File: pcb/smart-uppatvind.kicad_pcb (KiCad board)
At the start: 4 copper layers, 74 x 36 mm, 65 parts, among them J1 PWR, J2 QWIIC, J3 UART_PROG, J4 FAN, Q1 IRLML9301, Q2 MMBT3904, Q3 MMBT3904, Q4 MMBT3904, Q5 Q_NMOS_GSD, SW1 EN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

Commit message: Fixed inverted signals on main connectors, added generated schematic
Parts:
- moved JP1 6.28 mm to (82.5, 66.0), turned to 180 degrees
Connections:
- J1 pad 1: GNDPWR -> +24V
- J1 pad 2: +24V -> GNDPWR
- J4 pad 1: /FG -> /FAN_24V
- J4 pad 2: /PWM_5V -> GND
- J4 pad 3: GND -> /PWM_5V
- J4 pad 4: /FAN_24V -> /FG
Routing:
- net /FAN_24V: track 11.5 -> 5.27 mm
- net Net-(JP1-B): track 24.8 -> 27.8 mm
- net /PWM_5V: track 24.4 -> 22.0 mm
- net /FG: track 7.47 -> 6.42 mm
- net +24V: track 12.2 -> 12.3 mm, vias 2 -> 7

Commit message: Formatted some resistor values
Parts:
- R10, R20, R7, R9: value 330 R -> 330R
- R13, R17: value 5.1kR -> 5.1k
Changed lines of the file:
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@@
 			)
 		)
-		(property "Value" "330 R"
+		(property "Value" "330R"
 			(at 0 1.65 0)
 			(layer "F.Fab")
@@
 			)
 		)
-		(property "Value" "330 R"
+		(property "Value" "330R"
 			(at 0 1.65 0)
 			(layer "F.Fab")
@@
 			)
 		)
-		(property "Value" "330 R"
+		(property "Value" "330R"
 			(at 0 1.65 0)
 			(layer "F.Fab")
@@
 			)
 		)
-		(property "Value" "5.1kR"
+		(property "Value" "5.1k"
 			(at 0 1.65 90)
 			(layer "F.Fab")
@@
 			)
 		)
-		(property "Value" "330 R"
+		(property "Value" "330R"
 			(at 0 1.65 0)
 			(layer "F.Fab")
@@
 			)
 		)
-		(property "Value" "5.1kR"
+		(property "Value" "5.1k"
 			(at 0 1.65 90)
 			(layer "F.Fab")

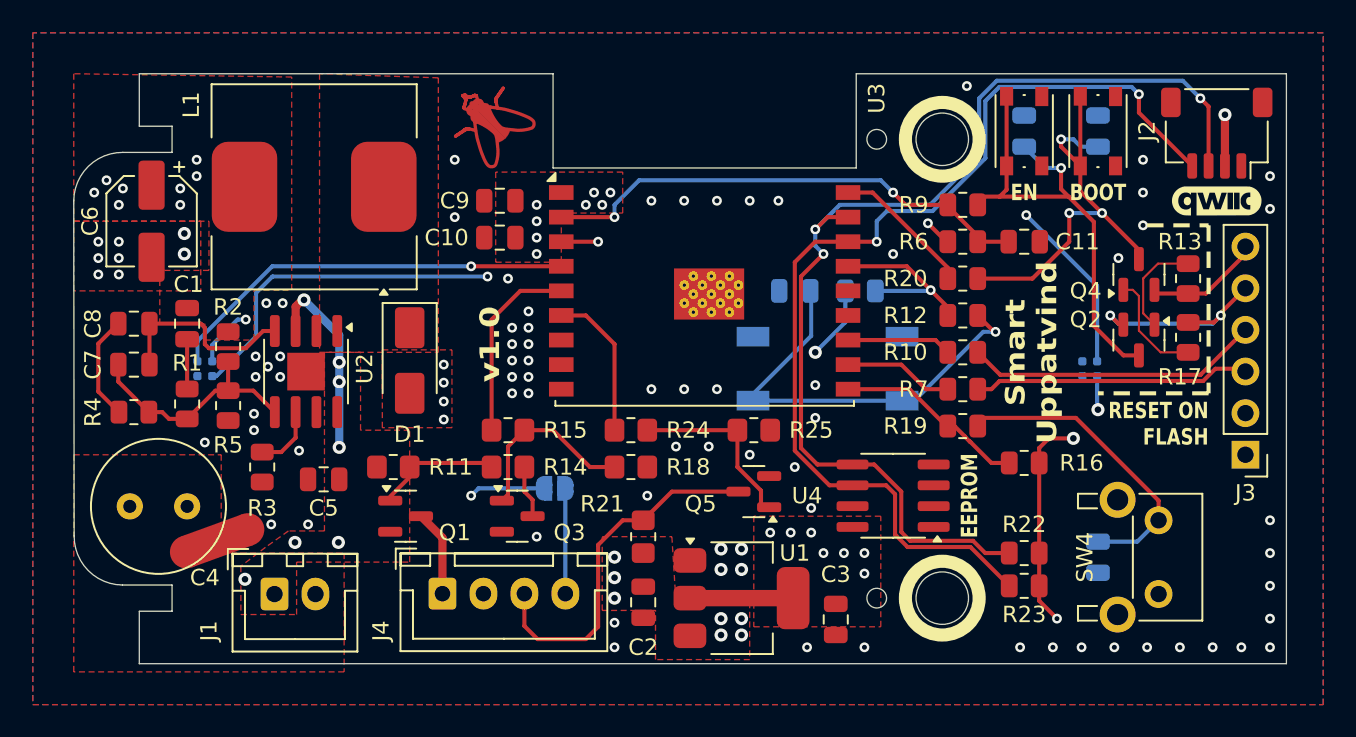
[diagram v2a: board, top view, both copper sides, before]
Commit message: Fixed incorrect connection of strapping pins for ESP32-C3
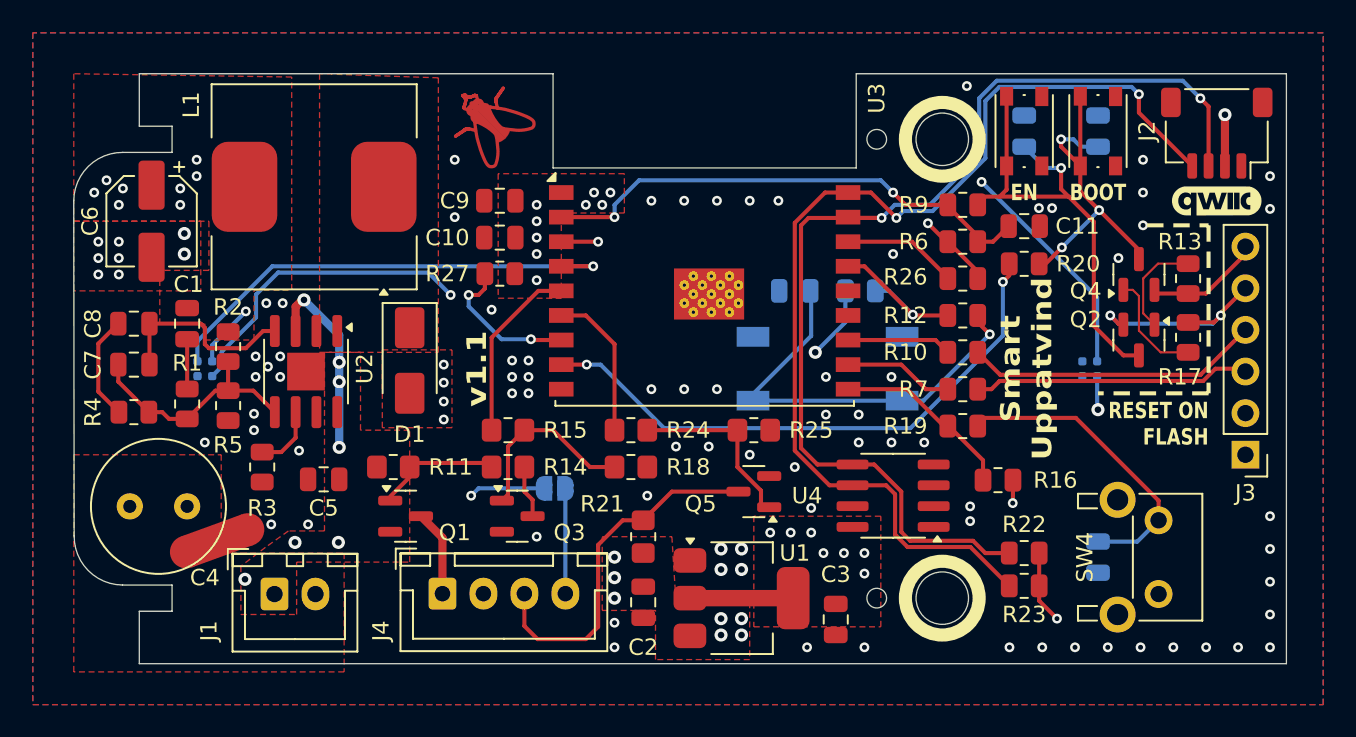
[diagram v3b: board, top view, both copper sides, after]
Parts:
- added R26: 100k, Resistor_SMD:R_0805_2012Metric, F.Cu at (107.3, 53.2)
- added R27: 100k, Resistor_SMD:R_0805_2012Metric, F.Cu at (79.1, 52.9)
- moved R20 3.86 mm to (111.1, 52.3)
- moved R16 1.91 mm to (109.5, 65.5)
- moved C11 0.95 mm to (111.1, 50.0)
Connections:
- U3 pad 16: /SCL -> Net-(U3-IO2)
- U3 pad 18: /BOOT -> /SCL
- U3 pad 7: unconnected-(U3-IO8-Pad7) -> Net-(U3-IO8)
- U3 pad 8: unconnected-(U3-IO9-Pad8) -> /BOOT
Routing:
- net /BOOT: track 8.15 -> 35.4 mm, vias 0 -> 2
- net Net-(U3-IO8): track 0.00 -> 9.26 mm, vias 0 -> 2
- net Net-(U3-IO2): track 0.00 -> 7.08 mm
- net Net-(Q4-C): track 25.7 -> 20.5 mm
- net VDD: track 28.7 -> 24.4 mm, vias 20 -> 21
- net /LED: track 25.3 -> 29.2 mm
- net /SCL: track 63.6 -> 65.5 mm
- net /FAN_EN: track 11.5 -> 10.8 mm
- net /EN: track 30.0 -> 30.6 mm
- net /SDA: vias 3 -> 2
- net GND: vias 73 -> 77
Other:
- board text removed: "EEPROM"

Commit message: Added back EEPROM text, cleaned up tracks
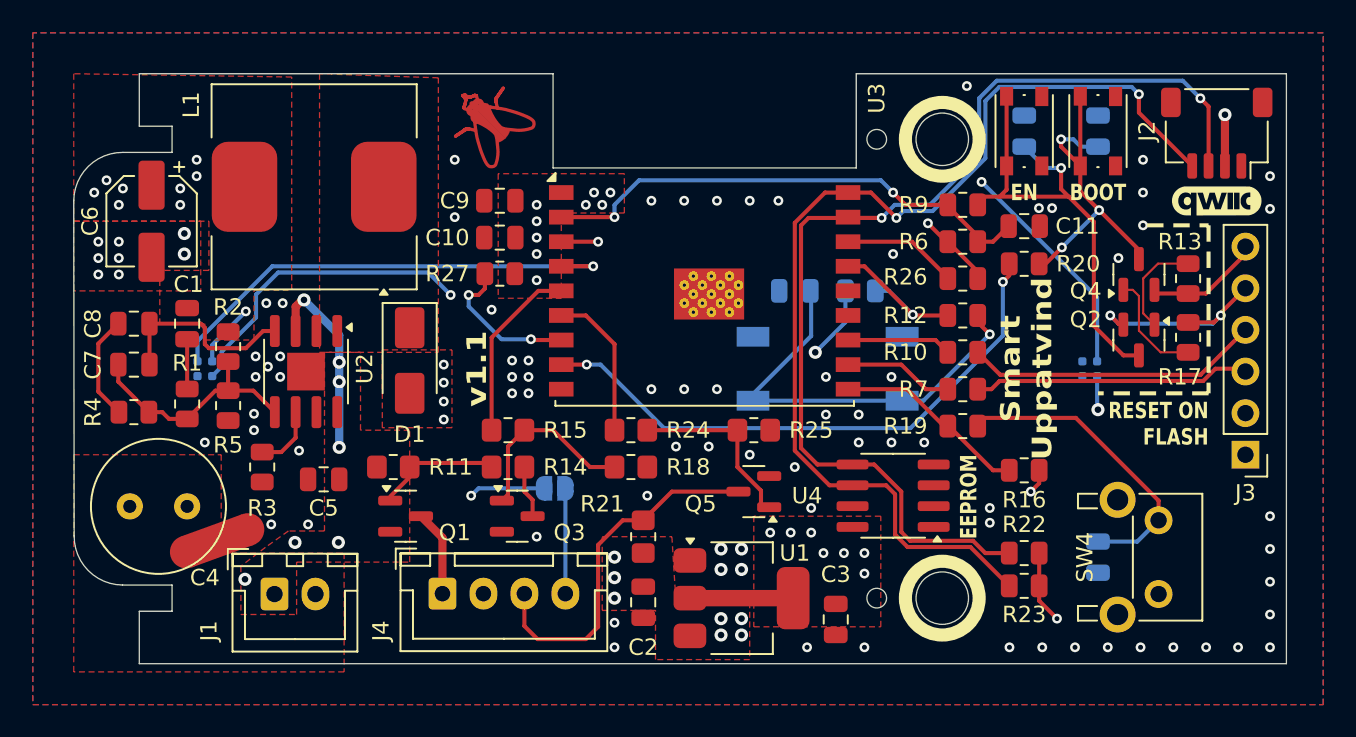
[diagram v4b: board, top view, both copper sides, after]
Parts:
- moved R16 1.71 mm to (111.1, 64.9)
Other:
- board text added: "EEPROM"
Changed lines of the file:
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@@
 			)
 		)
-		(attr board_only exclude_from_pos_files exclude_from_bom)
+		(attr board_only exclude_from_pos_files exclude_from_bom allow_missing_courtyard)
 		(fp_poly
 			(pts
@@
 	(footprint "Resistor_SMD:R_0805_2012Metric"
 		(layer "F.Cu")
-		(at 109.5 65.5 180)
+		(at 111.1 64.9 180)
 		(descr "Resistor SMD 0805 (2012 Metric), square (rectangular) end terminal, IPC_7351 nominal, (Body size source: IPC-SM-782 page 72, https://www.pcb-3d.com/wordpress/wp-content/uploads/ipc-sm-782a_amendment_1_and_2.pdf), generated with kicad-footprint-generator")
 		(tags "resistor")
 		(property "Reference" "R16"
-			(at -3.5 0 0)
+			(at 0 -1.8 0)
 			(layer "F.SilkS")
 			(effects
@@
 		)
 	)
+	(gr_text "EEPROM"
+		(at 108.3 66.515001 90)
+		(layer "F.SilkS")
+		(effects
+			(font
+				(size 1 0.8)
+				(thickness 0.2)
+				(bold yes)
+			)
+			(justify bottom)
+		)
+	)
 	(via
 		(at 86.1 72.7)
@@
 	)
 	(via
-		(at 107.8 67.1)
+		(at 109 67.2)
 		(size 0.6)
 		(drill 0.3)
@@
 	)
 	(via
-		(at 107.8 68)
+		(at 109 68.1)
 		(size 0.6)
 		(drill 0.3)
@@
 	)
 	(segment
-		(start 110.4125 65.5)
-		(end 110.4125 66.8875)
+		(start 112.0125 65.6875)
+		(end 112.0125 64.9)
 		(width 0.25)
 		(layer "F.Cu")
@@
 	)
 	(segment
-		(start 110.4125 66.8875)
-		(end 110.4 66.9)
-		(width 0.25)
-		(layer "F.Cu")
-		(net 4)
-	)
-	(segment
-		(start 108.3125 53.2)
-		(end 108.3125 52.825)
+		(start 111.5 66.2)
+		(end 112.0125 65.6875)
 		(width 0.25)
 		(layer "F.Cu")
@@
 	)
 	(via
+		(at 111.5 66.2)
+		(size 0.6)
+		(drill 0.3)
+		(layers "F.Cu" "B.Cu")
+		(free yes)
+		(net 4)
+	)
+	(via
 		(at 84.35 48.7)
 		(size 0.6)
@@
 	)
 	(via
-		(at 110.4 66.9)
-		(size 0.6)
-		(drill 0.3)
-		(layers "F.Cu" "B.Cu")
-		(net 4)
-	)
-	(via
 		(at 81.35 48.7)
 		(size 0.6)
@@
 	)
 	(segment
-		(start 67.1 54.45)
-		(end 67.15 54.5)
-		(width 0.5)
-		(layer "B.Cu")
-		(net 5)
-	)
-	(segment
 		(start 67.15 54.5)
 		(end 69.3 56.65)
@@
 	)
 	(segment
-		(start 67.1 54.45)
-		(end 67.1 54.45)
-		(width 0.5)
-		(layer "B.Cu")
-		(net 5)
-	)
-	(segment
 		(start 69.3 56.65)
 		(end 69.3 58.3)
@@
 	)
 	(segment
-		(start 110.15 50)
-		(end 110.15 50.2)
-		(width 0.25)
-		(layer "F.Cu")
-		(net 10)
-	)
-	(segment
 		(start 109.2 50.95)
 		(end 110.15 50)
@@
 	)
 	(segment
-		(start 108.2625 55.8625)
-		(end 108.2625 55.45)
-		(width 0.25)
-		(layer "F.Cu")
-		(net 11)
-	)
-	(segment
 		(start 109 56.6)
 		(end 108.2625 55.8625)
@@
 	)
 	(segment
-		(start 112.2 52.5)
-		(end 112.0125 52.5)
-		(width 0.25)
-		(layer "F.Cu")
-		(net 13)
-	)
-	(segment
 		(start 113.35 45.15)
 		(end 114.525 46.325)
@@
 	)
 	(segment
-		(start 100.4 49.5)
-		(end 100.35 49.45)
-		(width 0.25)
-		(layer "F.Cu")
-		(net 20)
-	)
-	(segment
 		(start 104.137402 69.2)
 		(end 103.6 68.662598)
@@
 	)
 	(segment
-		(start 106.4375 62.2)
-		(end 106.2 62.2)
-		(width 0.25)
-		(layer "F.Cu")
-		(net 40)
-	)
-	(segment
-		(start 108.5875 64.2875)
-		(end 108.5875 65.5)
+		(start 109.2 64.9)
+		(end 110.1875 64.9)
 		(width 0.25)
 		(layer "F.Cu")
@@
 	(segment
 		(start 106.5 62.2)
-		(end 108.5875 64.2875)
-		(width 0.25)
-		(layer "F.Cu")
-		(net 40)
-	)
-	(segment
-		(start 106.4375 62.2)
-		(end 106.5 62.2)
+		(end 109.2 64.9)
 		(width 0.25)
 		(layer "F.Cu")
@@
 	)
 	(segment
-		(start 106.4875 53.2)
-		(end 106.4875 53.1875)
-		(width 0.25)
-		(layer "F.Cu")
-		(net 45)
-	)
-	(segment
 		(start 106.4875 53.1875)
 		(end 104.25 50.95)
@@
 	)
 	(zone
+		(net 41)
+		(net_name "/BOOT")
+		(layer "F.Cu")
+		(name "$teardrop_padvia$")
+		(hatch full 0.1)
+		(priority 30000)
+		(attr
+			(teardrop
+				(type padvia)
+			)
+		)
+		(connect_pads yes
+			(clearance 0)
+		)
+		(min_thickness 0.0254)
+		(filled_areas_thickness no)
+		(fill yes
+			(thermal_gap 0.5)
+			(thermal_bridge_width 0.5)
+			(island_removal_mode 1)
+			(island_area_min 10)
+		)
+		(polygon
+			(pts
+				(xy 109.745559 53.277665) (xy 109.922335 53.454441) (xy 110.49875 52.990302) (xy 110.188207 52.299293)
+				(xy 109.675 52.75)
+			)
+		)
+	)
+	(zone
 		(net 1)
 		(net_name "+5V")
@@
 			)
 		)
-	)
-	(zone
-		(net 41)
-		(net_name "/BOOT")
-		(layer "F.Cu")
-		(name "$teardrop_padvia$")
-		(hatch full 0.1)
-		(priority 30000)
-		(attr
-			(teardrop
-				(type padvia)
-			)
-		)
-		(connect_pads yes
-			(clearance 0)
-		)
-		(min_thickness 0.0254)
-		(filled_areas_thickness no)
-		(fill yes
-			(thermal_gap 0.5)
-			(thermal_bridge_width 0.5)
-			(island_removal_mode 1)
-			(island_area_min 10)
-		)
-		(polygon
-			(pts
-				(xy 109.745559 53.277665) (xy 109.922335 53.454441) (xy 110.49875 52.990302) (xy 110.188207 52.299293)
-				(xy 109.675 52.75)
-			)
-		)

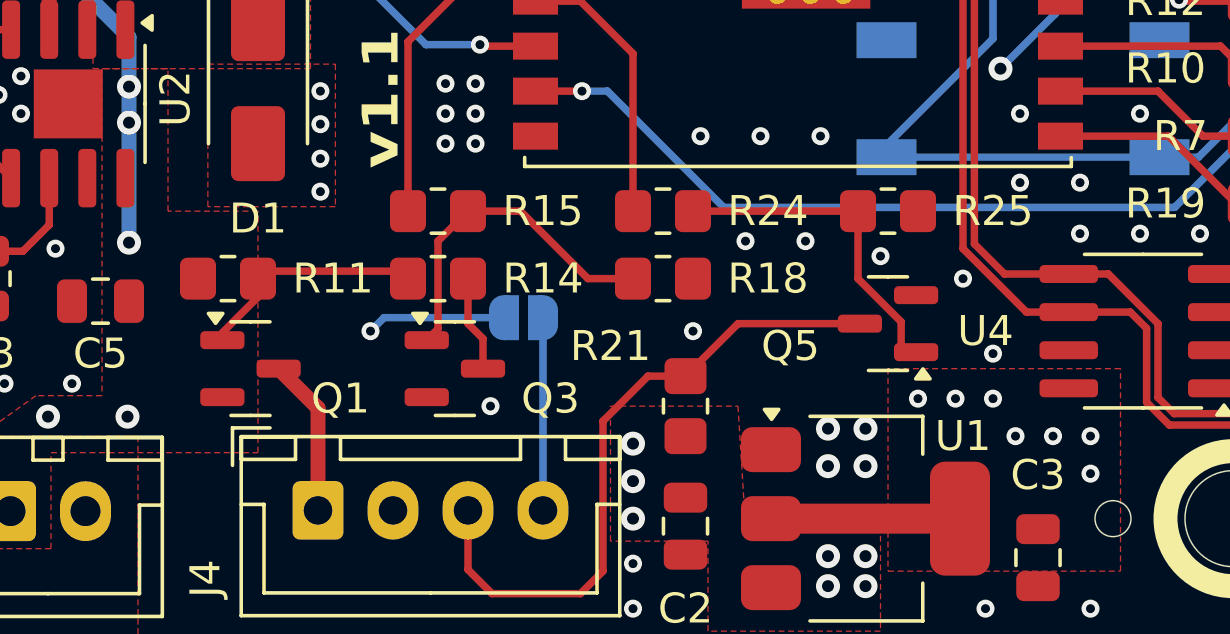
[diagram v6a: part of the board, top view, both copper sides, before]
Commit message: Unified resistor footprints - removed handsolder variants
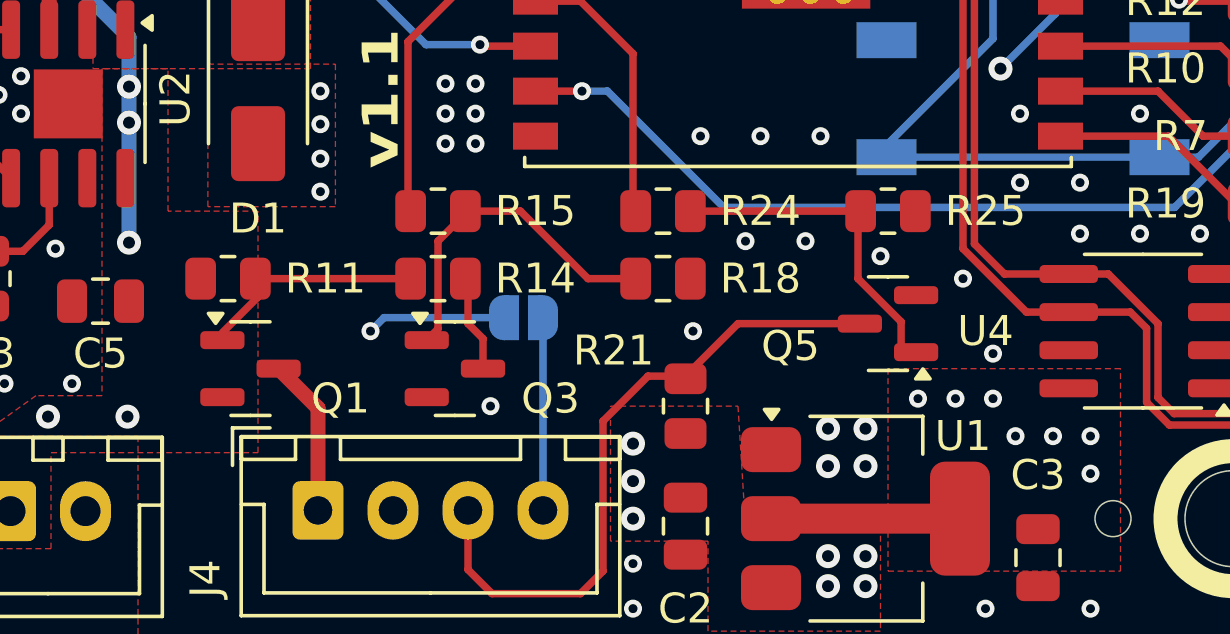
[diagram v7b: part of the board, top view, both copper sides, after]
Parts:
- R11, R14, R15, R18, R21, R25: footprint Resistor_SMD:R_0805_2012Metric_Pad1.20x1.40mm_HandSolder -> Resistor_SMD:R_0805_2012Metric
- R24: value 120R -> 150R; footprint Resistor_SMD:R_0805_2012Metric_Pad1.20x1.40mm_HandSolder -> Resistor_SMD:R_0805_2012Metric

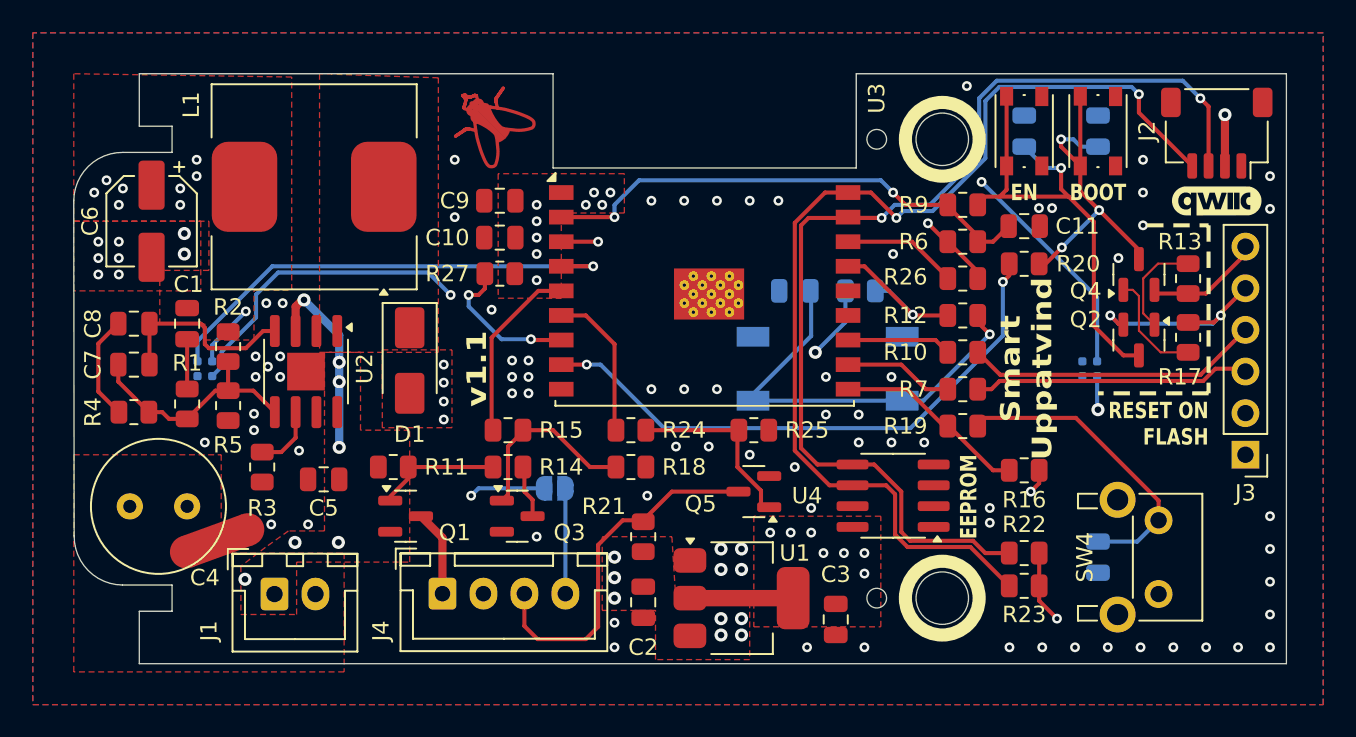
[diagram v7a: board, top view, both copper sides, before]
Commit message: Optimized routing
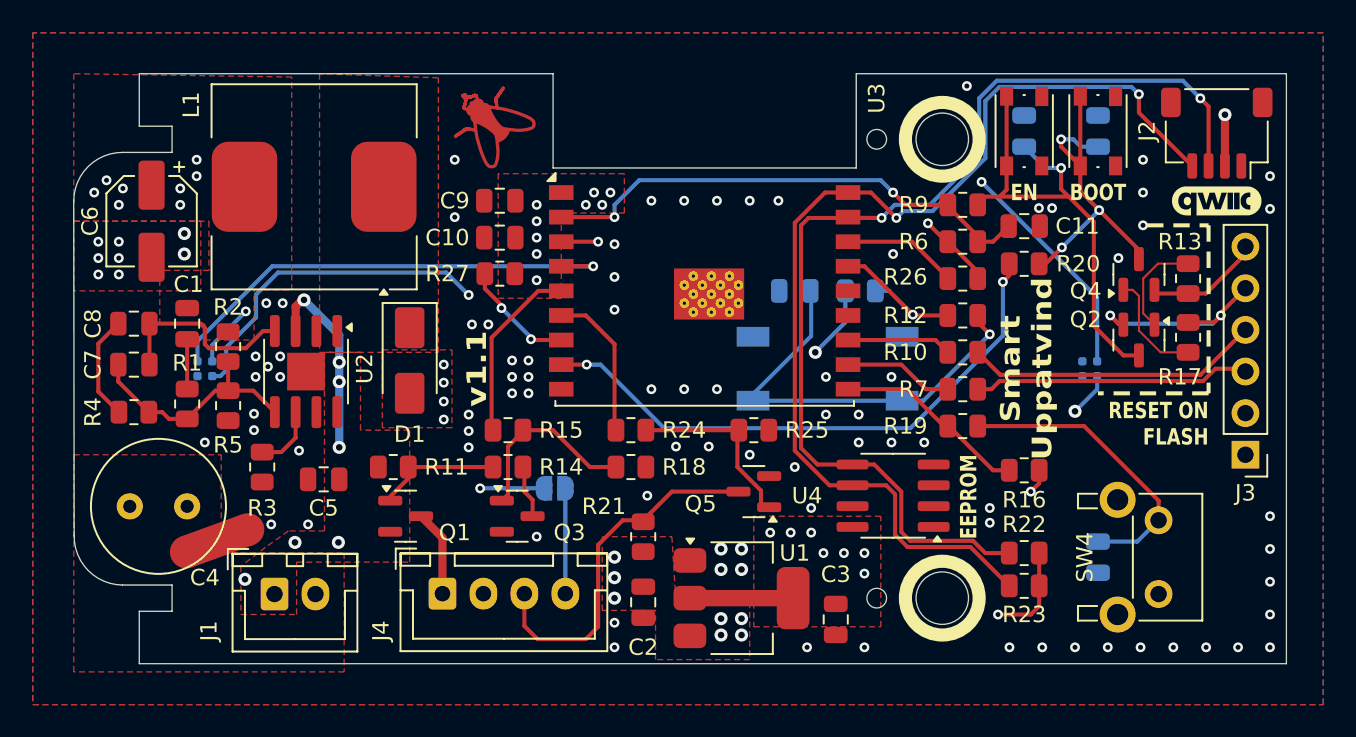
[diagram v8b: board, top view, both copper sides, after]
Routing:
- net +5V: track 39.3 -> 6.61 mm
- net Net-(JP1-B): track 27.8 -> 24.2 mm
- net Net-(U3-IO8): track 9.26 -> 7.04 mm
- net VDD: track 24.1 -> 25.7 mm
- net Net-(D2-DOUT): track 69.5 -> 70.5 mm
- net GND: vias 77 -> 84
